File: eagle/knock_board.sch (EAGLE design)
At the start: 21 parts, among them U2 TLC2262CP, U3 ATTINY25V-10PU

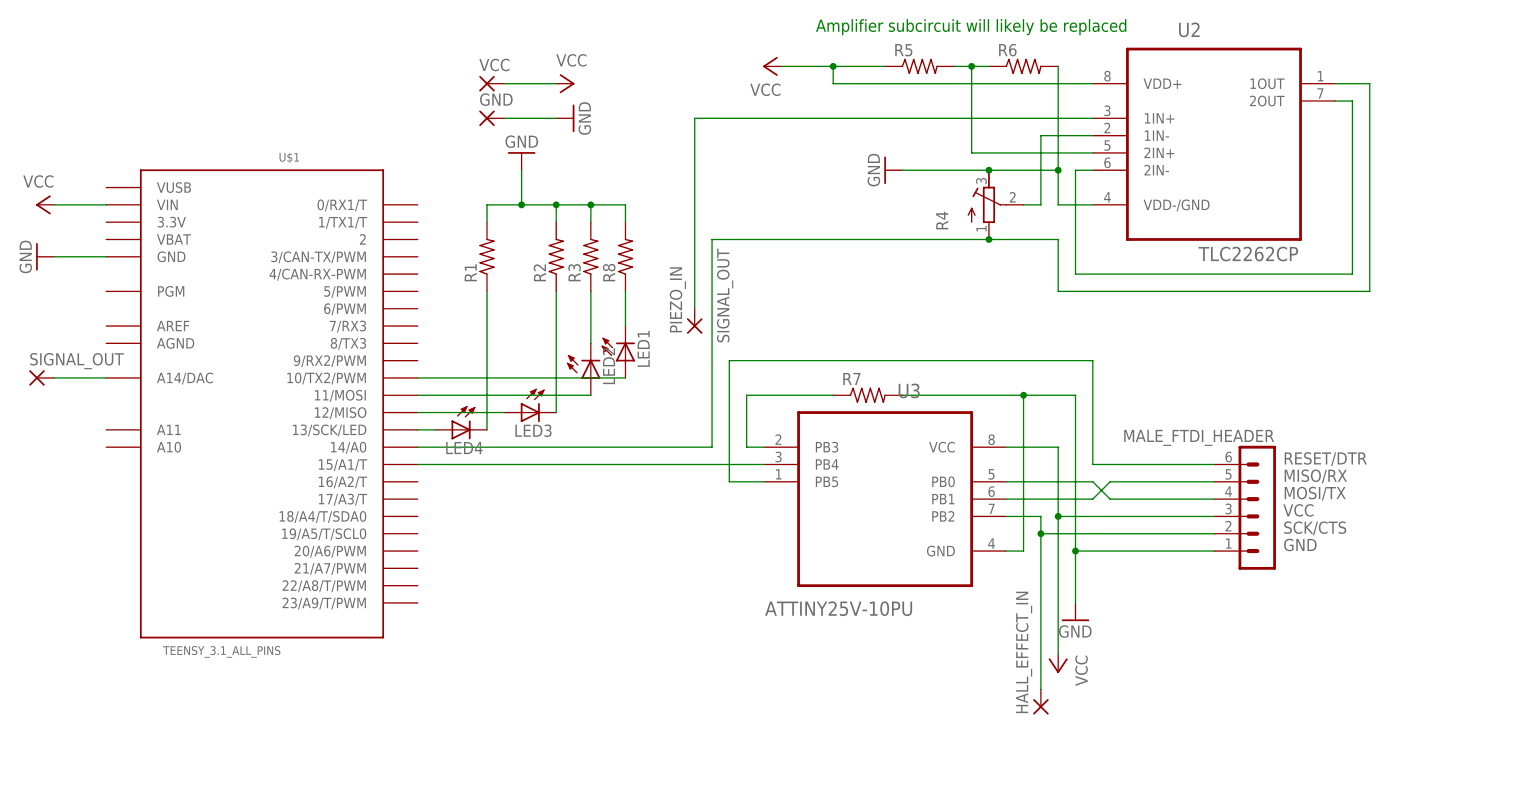
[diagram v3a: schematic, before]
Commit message: update amplifier schematic and change overflow counter from uint8 to uint16
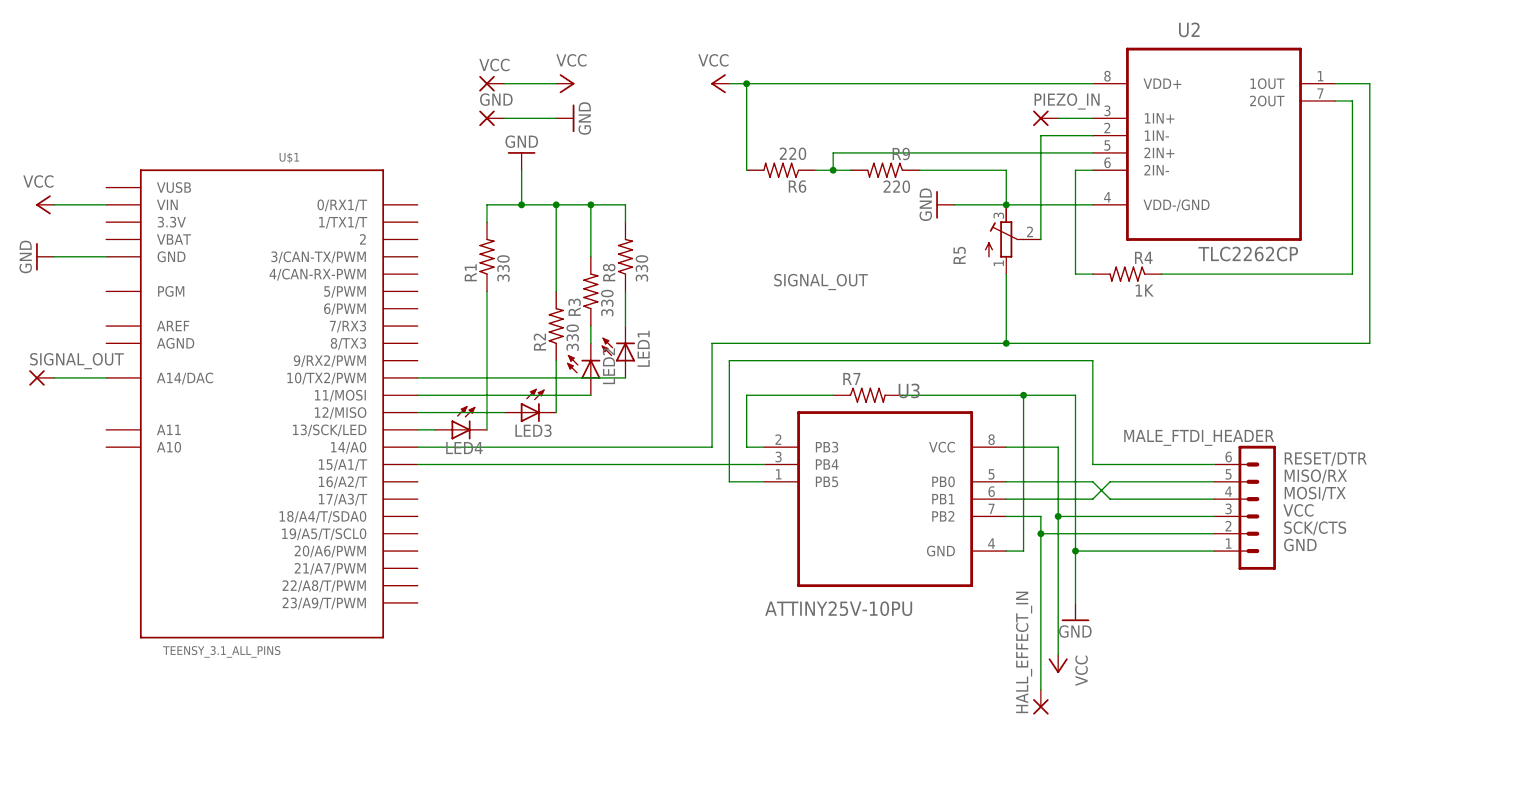
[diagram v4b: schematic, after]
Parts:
- added R9: 220, rcl:R-US_0204/5
- R1, R2, R3, R8: value (none) -> 330
- R4: value (none) -> 1K; device resistor:R-TRIMM3296W -> rcl:R-US_0204/5
- R5: device rcl:R-US_0204/5 -> rcl:R-TRIMM4G/J
- R6: value (none) -> 220
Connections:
- new net N$15: R4.1, U2.2OUT
- net GND: now also R5.E, R9.1; no longer R4.E, R6.2
- net N$3: now also R5.S; no longer R4.S
- net N$4: now also R4.2; no longer U2.2OUT
- net N$6: now also R9.2; no longer R5.2
- net SIGNAL_OUT: now also R5.A; no longer R4.A
- net VCC: now also R6.2; no longer R5.1
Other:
- note removed: "Amplifier subcircuit will likely be replaced"
- moved on the sheet: PIEZO_IN, R2, R3, R6
